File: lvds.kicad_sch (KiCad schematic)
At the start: 33 parts, among them J4 Conn_01x15_Female, J9 Conn_01x34_Female, U10 TPS61176RTER, U11 TCA9802, U12 NTB0102, U13 MIC5504-1.8YM5, U5 SN65DSI83TPAPRQ1

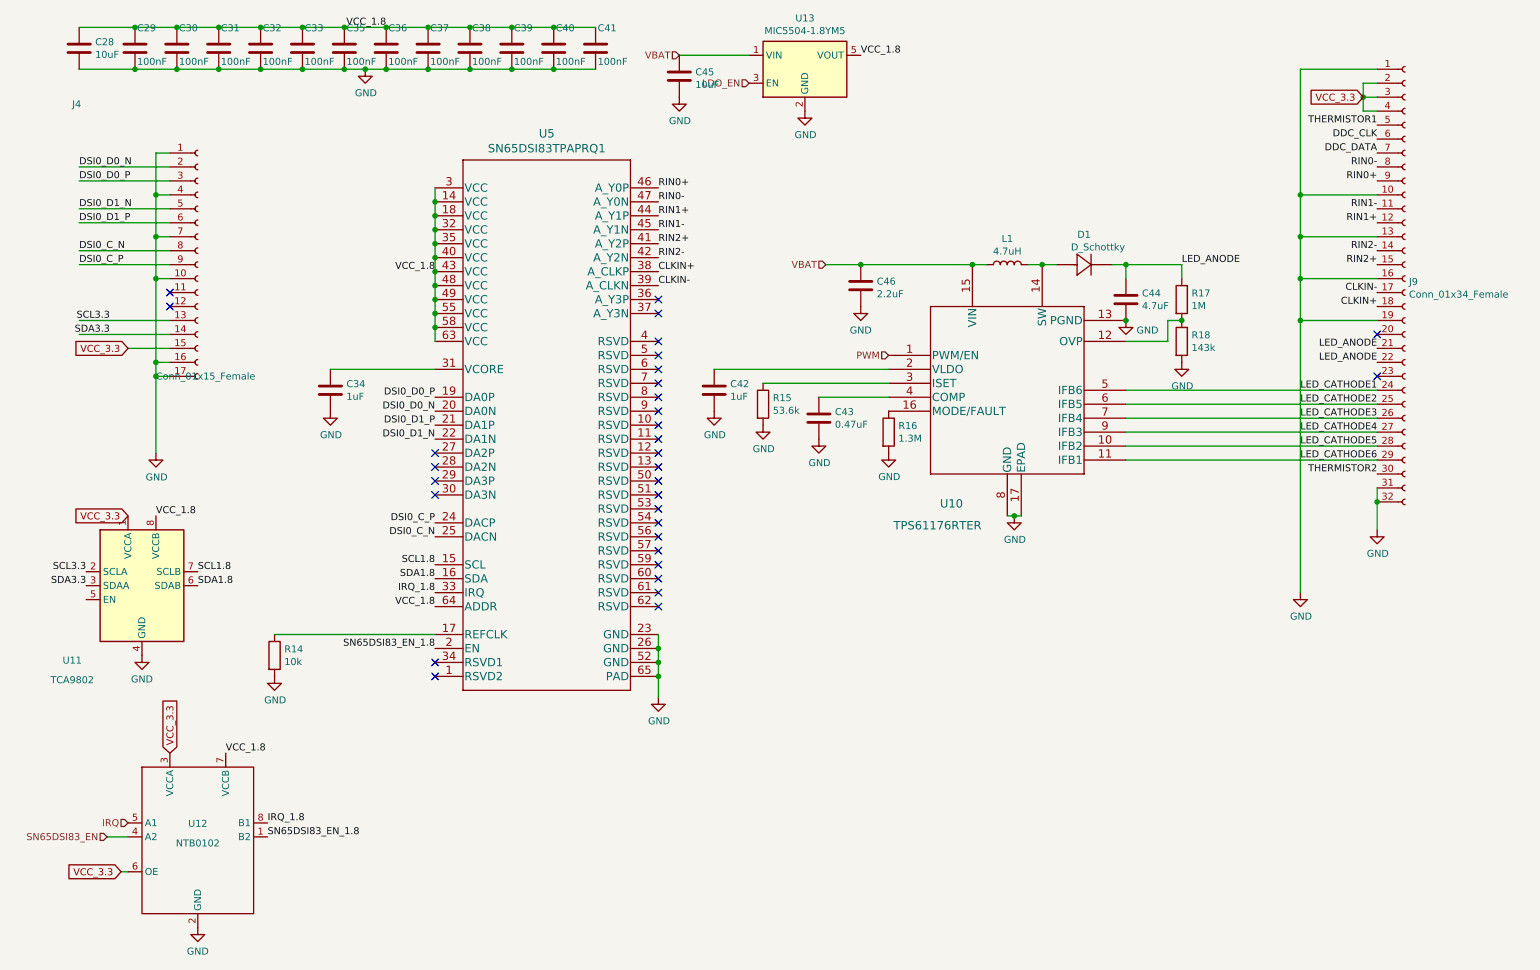
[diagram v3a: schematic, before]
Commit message: Fix (or ignore) all ERC and DRC errors.
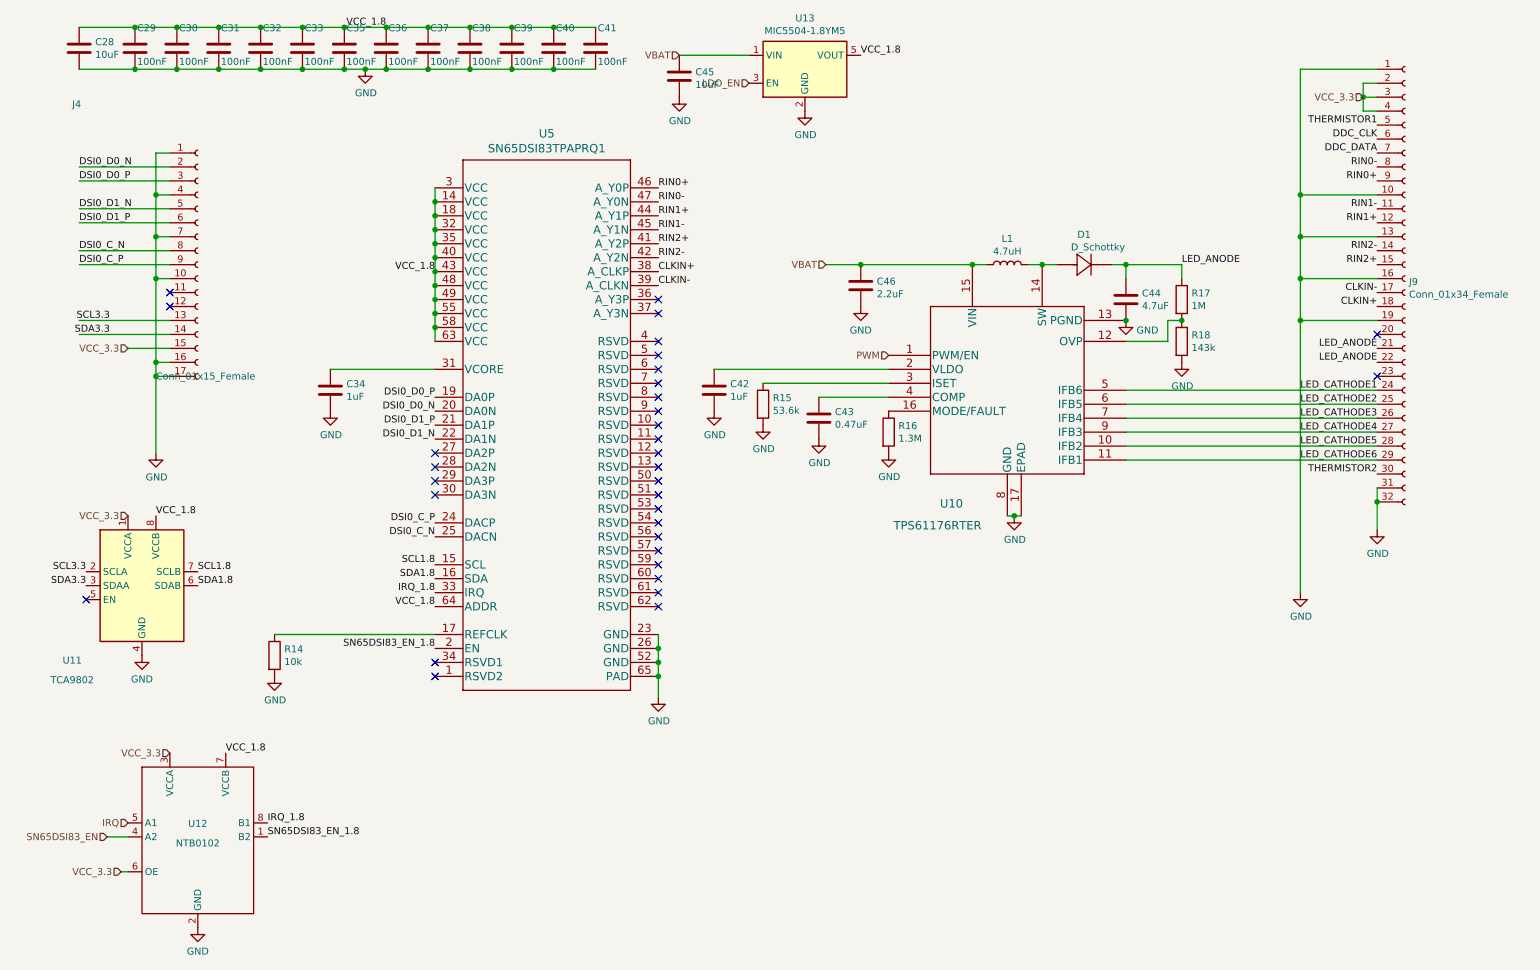
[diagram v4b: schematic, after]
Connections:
- no-connect marks 32 -> 33
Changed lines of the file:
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@@
   (junction (at 259.08 34.29) (diameter 1.016) (color 0 0 0 0))
   (junction (at 261.62 107.95) (diameter 1.016) (color 0 0 0 0))
+  (no_connect (at 26.67 125.73))
   (no_connect (at 41.91 69.85))
   (no_connect (at 41.91 72.39))
@@
     (effects (font (size 1.27 1.27)) (justify right bottom))
   )
-  (global_label "VCC_3.3" (shape input) (at 33.02 175.26 180)
-    (effects (font (size 1.27 1.27)) (justify right))
-    (property "Intersheet References" "${INTERSHEET_REFS}" (id 0) (at 22.9869 175.1806 0)
-      (effects (font (size 1.27 1.27)) (justify right) hide)
-    )
-  )
-  (global_label "VCC_3.3" (shape input) (at 34.29 80.01 180)
-    (effects (font (size 1.27 1.27)) (justify right))
-    (property "Intersheet References" "${INTERSHEET_REFS}" (id 0) (at 24.2569 79.9306 0)
-      (effects (font (size 1.27 1.27)) (justify right) hide)
-    )
-  )
-  (global_label "VCC_3.3" (shape input) (at 34.29 110.49 180)
-    (effects (font (size 1.27 1.27)) (justify right))
-    (property "Intersheet References" "${INTERSHEET_REFS}" (id 0) (at 24.2569 110.4106 0)
-      (effects (font (size 1.27 1.27)) (justify right) hide)
-    )
-  )
-  (global_label "VCC_3.3" (shape input) (at 41.91 153.67 90)
-    (effects (font (size 1.27 1.27)) (justify left))
-    (property "Intersheet References" "${INTERSHEET_REFS}" (id 0) (at 41.9894 143.6369 90)
-      (effects (font (size 1.27 1.27)) (justify left) hide)
-    )
-  )
-  (global_label "VCC_3.3" (shape input) (at 259.08 34.29 180)
-    (effects (font (size 1.27 1.27)) (justify right))
-    (property "Intersheet References" "${INTERSHEET_REFS}" (id 0) (at 249.0469 34.2106 0)
-      (effects (font (size 1.27 1.27)) (justify right) hide)
-    )
-  )
   (hierarchical_label "SN65DSI83_EN" (shape input) (at 30.48 168.91 180)
     (effects (font (size 1.27 1.27)) (justify right))
   )
+  (hierarchical_label "VCC_3.3" (shape input) (at 33.02 175.26 180)
+    (effects (font (size 1.27 1.27)) (justify right))
+  )
+  (hierarchical_label "VCC_3.3" (shape input) (at 34.29 80.01 180)
+    (effects (font (size 1.27 1.27)) (justify right))
+  )
+  (hierarchical_label "VCC_3.3" (shape input) (at 34.29 110.49 180)
+    (effects (font (size 1.27 1.27)) (justify right))
+  )
   (hierarchical_label "IRQ" (shape input) (at 34.29 166.37 180)
     (effects (font (size 1.27 1.27)) (justify right))
   )
+  (hierarchical_label "VCC_3.3" (shape input) (at 41.91 153.67 180)
+    (effects (font (size 1.27 1.27)) (justify right))
+  )
   (hierarchical_label "VBAT" (shape input) (at 134.62 26.67 180)
     (effects (font (size 1.27 1.27)) (justify right))
@@
     (effects (font (size 1.27 1.27)) (justify right))
   )
+  (hierarchical_label "VCC_3.3" (shape input) (at 259.08 34.29 180)
+    (effects (font (size 1.27 1.27)) (justify right))
+  )

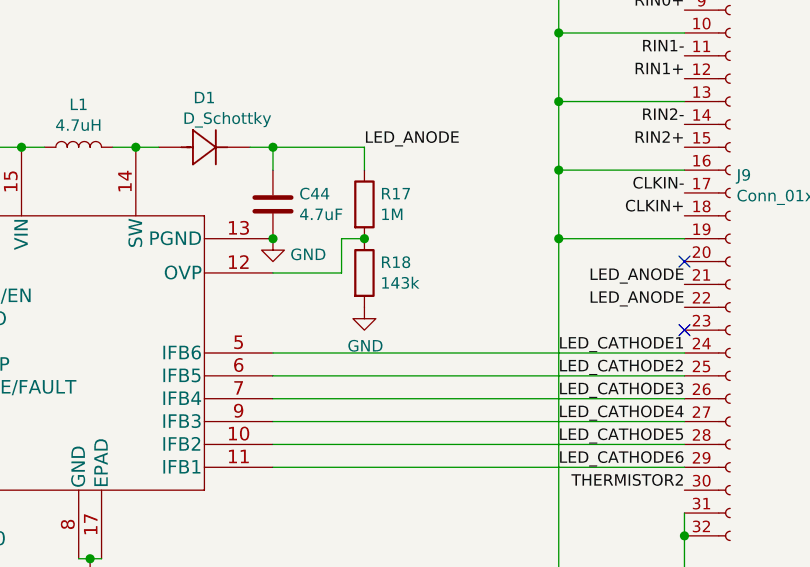
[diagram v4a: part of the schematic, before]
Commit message: Change R18 to 82k so LCD backlight controller can be up to 19.8V, instead of 12V. Add script for reading and parsing bq25895 registers. Add datasheets for samsung-produced LCD panels.
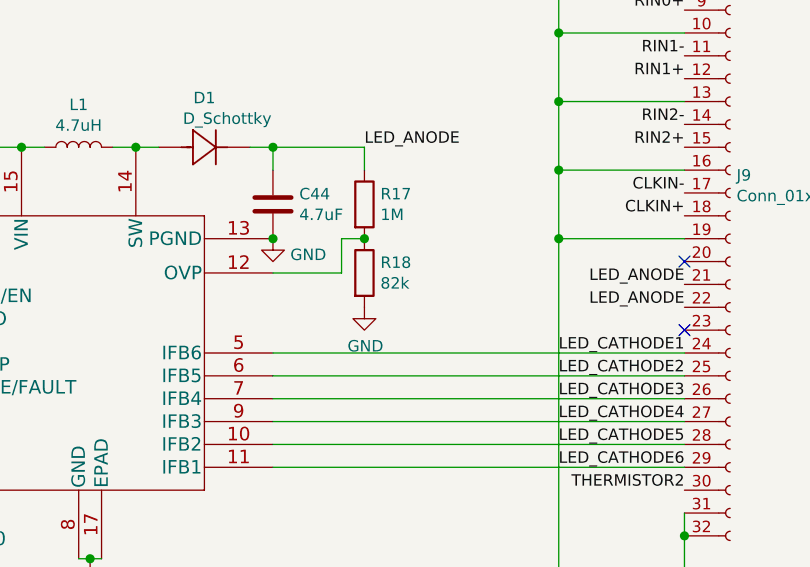
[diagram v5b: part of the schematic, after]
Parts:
- R18: value 143k -> 82k
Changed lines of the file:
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@@
       (effects (font (size 1.27 1.27)) (justify left))
     )
-    (property "Value" "143k" (id 1) (at 227.838 79.889 0)
+    (property "Value" "82k" (id 1) (at 227.838 79.889 0)
       (effects (font (size 1.27 1.27)) (justify left))
     )

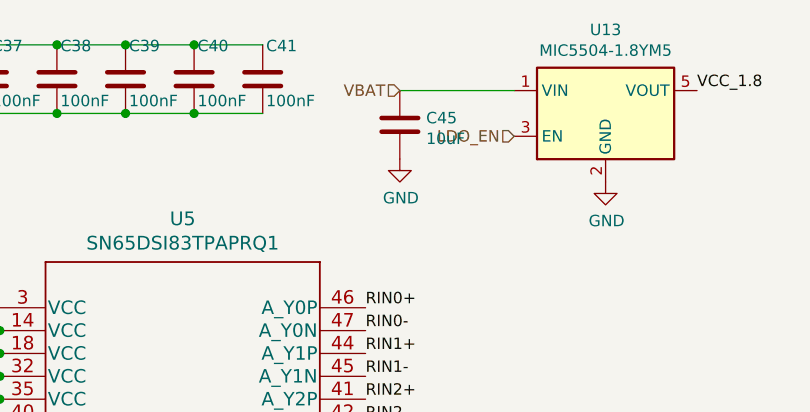
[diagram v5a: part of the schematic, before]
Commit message: Fix footprint for FSA2275. Fixes #13
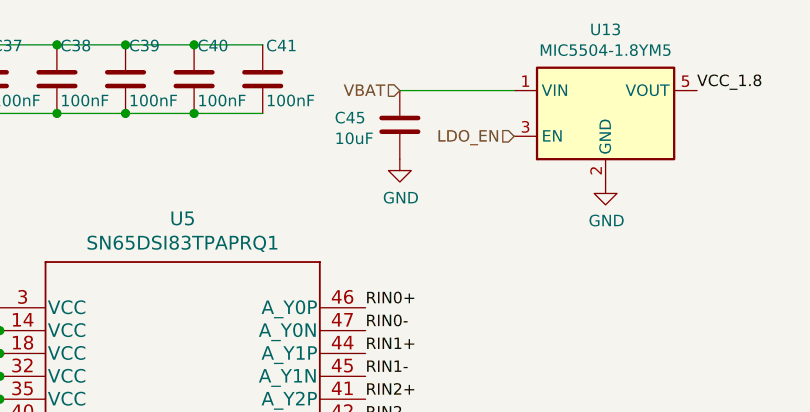
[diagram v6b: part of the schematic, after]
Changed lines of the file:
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@@
   )
   (symbol (lib_id "Device:C") (at 134.62 30.48 0) (unit 1)
-    (in_bom yes) (on_board yes) (fields_autoplaced)
-    (property "Reference" "C45" (id 0) (at 137.5411 29.7191 0)
+    (in_bom yes) (on_board yes)
+    (property "Reference" "C45" (id 0) (at 127.3811 29.7191 0)
       (effects (font (size 1.27 1.27)) (justify left))
     )
-    (property "Value" "10uF" (id 1) (at 137.5411 32.0178 0)
+    (property "Value" "10uF" (id 1) (at 127.3811 32.0178 0)
       (effects (font (size 1.27 1.27)) (justify left))
     )

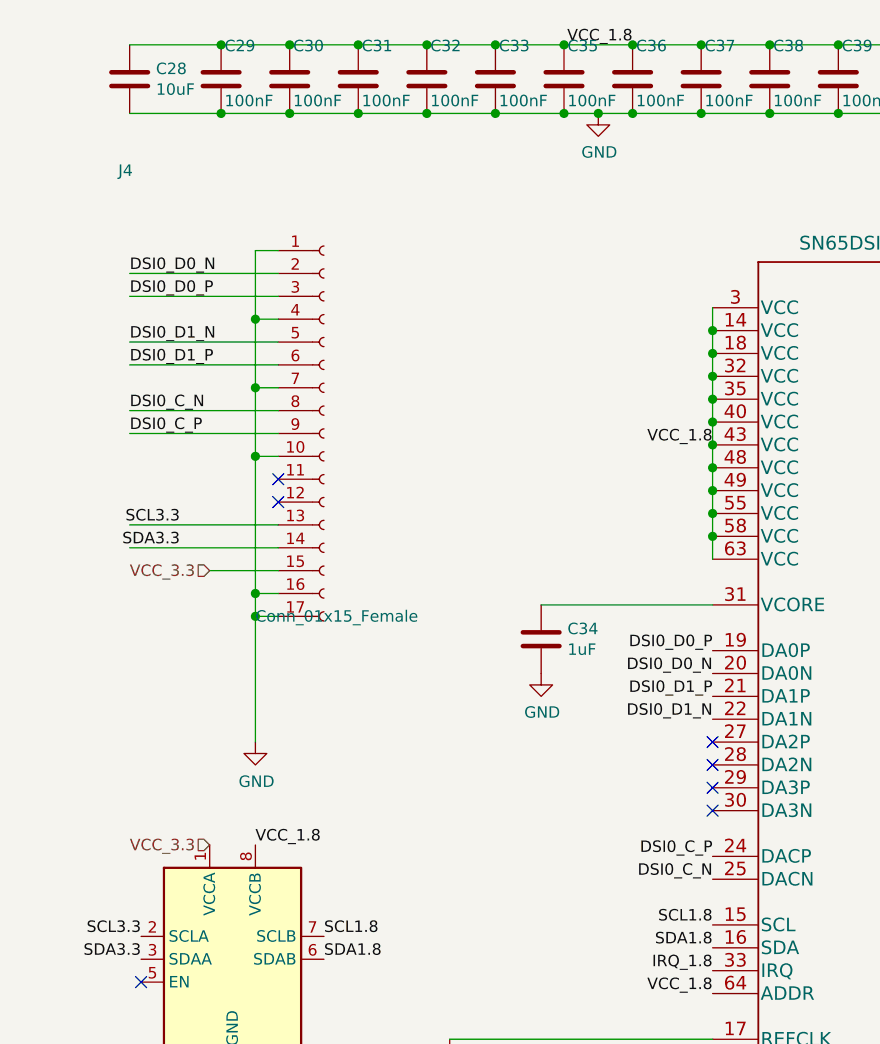
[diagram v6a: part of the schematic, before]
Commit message: WIP: start reworking board to use CM4 instead of 40-pin connector
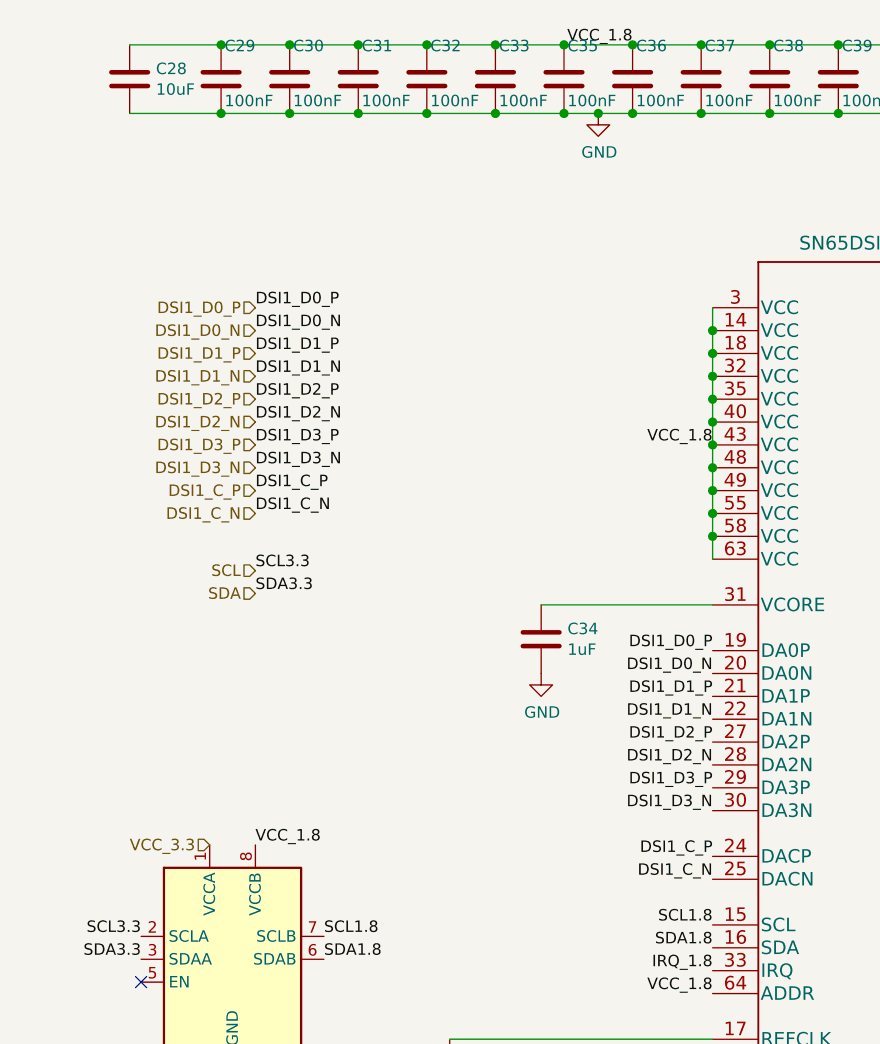
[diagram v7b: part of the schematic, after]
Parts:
- removed J4: Conn_01x15_Female, footprints:SFW15R-2STE1LF, symbol Connector:Conn_01x17_Female
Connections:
- net DSI1_D2_P: now reaches U5.27 (DA2P)
- net DSI1_D2_N: now reaches U5.28 (DA2N)
- net DSI1_D3_P: now reaches U5.29 (DA3P)
- net DSI1_D3_N: now reaches U5.30 (DA3N)
- net DSI0_C_N renamed DSI1_C_N
- net DSI0_C_P renamed DSI1_C_P
- net DSI0_D0_N renamed DSI1_D0_N
- net DSI0_D0_P renamed DSI1_D0_P
- net DSI0_D1_N renamed DSI1_D1_N
- net DSI0_D1_P renamed DSI1_D1_P
- net SCL3.3 renamed SCL
- net SDA3.3 renamed SDA
- no-connect marks 33 -> 27

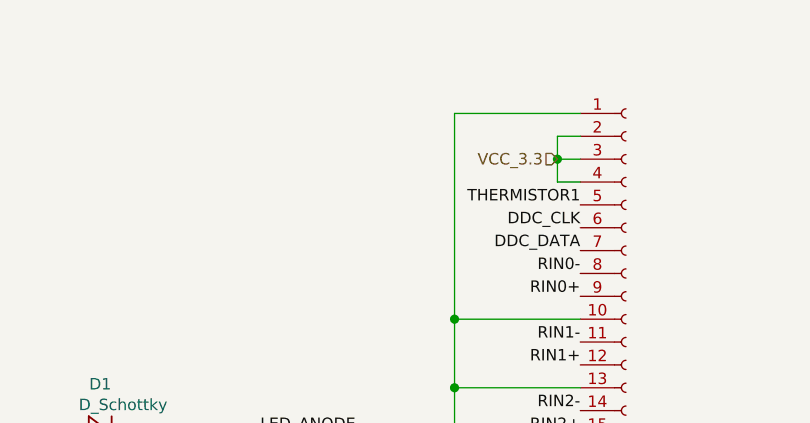
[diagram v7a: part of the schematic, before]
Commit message: reroute LVDS diff pairs; add 5v boost converter. Fixes #1.
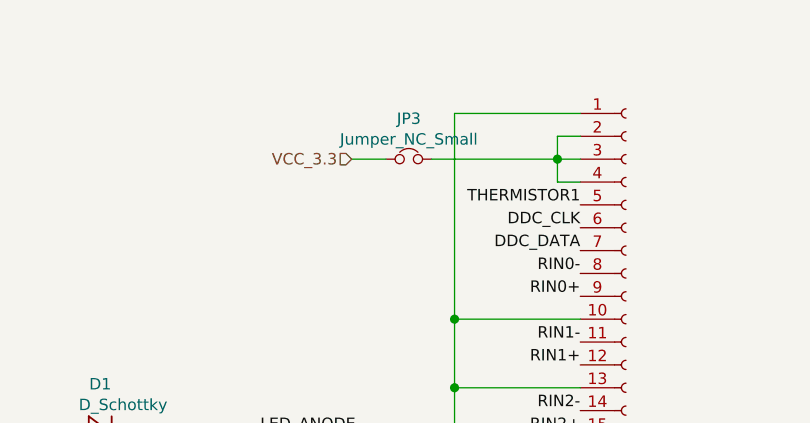
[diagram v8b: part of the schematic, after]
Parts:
- added JP3: Jumper_NC_Small, Resistor_SMD:R_0402_1005Metric, symbol Device:Jumper_NC_Small
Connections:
- net VCC_3.3: now also JP3.1; no longer J9.2 (Pin_2), J9.3 (Pin_3), J9.4 (Pin_4)
- new net: J9.2 (Pin_2), J9.3 (Pin_3), J9.4 (Pin_4), JP3.2
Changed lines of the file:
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@@
+    (stroke (width 0) (type solid) (color 0 0 0 0))
+  )
+  (wire (pts (xy 236.22 34.29) (xy 240.03 34.29))
+    (stroke (width 0) (type solid) (color 0 0 0 0))
+  )
+  (wire (pts (xy 245.11 34.29) (xy 259.08 34.29))
     (stroke (width 0) (type solid) (color 0 0 0 0))
   )
@@
     (effects (font (size 1.27 1.27)) (justify right))
   )
-  (hierarchical_label "VCC_3.3" (shape input) (at 259.08 34.29 180)
+  (hierarchical_label "VCC_3.3" (shape input) (at 236.22 34.29 180)
     (effects (font (size 1.27 1.27)) (justify right))
   )
@@
       (effects (font (size 1.27 1.27)) hide)
     )
+    (pin "1")
+    (pin "2")
+  )
+  (symbol (lib_id "Device:Jumper_NC_Small") (at 242.57 34.29 0) (unit 1)
+    (in_bom yes) (on_board yes) (fields_autoplaced)
+    (property "Reference" "JP3" (id 0) (at 242.57 29.79 0))
+    (property "Value" "Jumper_NC_Small" (id 1) (at 242.57 32.0887 0))
+    (property "Footprint" "Resistor_SMD:R_0402_1005Metric" (id 2) (at 242.57 34.29 0)
+      (effects (font (size 1.27 1.27)) hide)
+    )
+    (property "Datasheet" "~" (id 3) (at 242.57 34.29 0)
+      (effects (font (size 1.27 1.27)) hide)
+    )
